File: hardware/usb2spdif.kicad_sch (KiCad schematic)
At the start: 18 parts, among them J1 USB_C_Receptacle_USB2.0_16P, U1 RP2040, U2 W25Q16JVSS, U3 AP130-33Y, Y1 12MHz

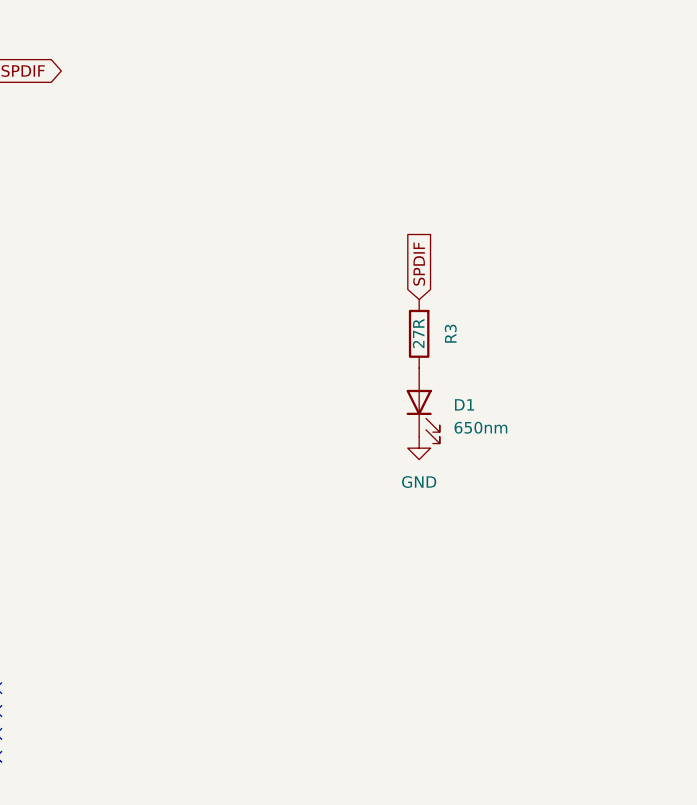
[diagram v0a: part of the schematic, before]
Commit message: [PCB] add real toslink TX and S/PDIF coax to schematic
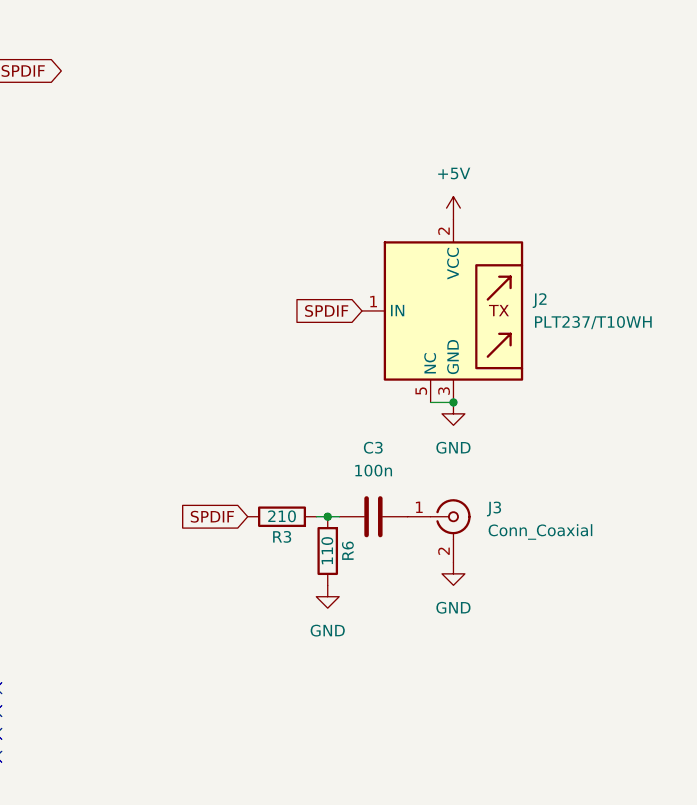
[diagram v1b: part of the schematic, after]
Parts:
- removed D1: 650nm, LED_THT:LED_D3.0mm_Horizontal_O1.27mm_Z2.0mm_Clear, symbol Device:LED
- added C3: 100n, symbol Device:C
- added J2: PLT237/T10WH, symbol spdif_tx:EVERLIGHT PLT237/T10WH
- added J3: Conn_Coaxial, symbol Connector:Conn_Coaxial
- added R6: 110, Resistor_SMD:R_0603_1608Metric, symbol Device:R
- R3: value 27R -> 210
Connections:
- net +5V: now also J2.2 (VCC)
- net GND: now also J2.3 (GND), J2.4 (NC), J2.5 (NC), J3.2 (Ext), R6.1
- net SPDIF: now also R3.1, J2.1 (IN); no longer R3.2
- new net: C3.1, R3.2, R6.2
- new net: C3.2, J3.1 (In)

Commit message: [PCB] forgot to commit that
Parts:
- added SW1: TS-1088-xR025, Button_Switch_SMD:SW_SPST_TS-1088-xR025, symbol Switch:SW_Push
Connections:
- net FLASH_CS: now also SW1.2
- net GND: now also SW1.1
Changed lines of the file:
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@@
+	(wire
+		(pts
+			(xy 58.42 185.42) (xy 49.53 185.42)
+		)
+		(stroke
+			(width 0)
+			(type default)
+		)
+	)
 	(wire
 		(pts
@@
 		)
 	)
+	(label "FLASH_CS"
+		(at 58.42 185.42 180)
+		(effects
+			(font
+				(size 1.27 1.27)
+			)
+			(justify right bottom)
+		)
+	)
 	(label "FLASH_CK"
 		(at 66.04 100.33 180)
@@
 	)
 	(symbol
+		(lib_id "power:GND")
+		(at 39.37 185.42 270)
+		(unit 1)
+		(exclude_from_sim no)
+		(in_bom yes)
+		(on_board yes)
+		(dnp no)
+		(fields_autoplaced yes)
+		(property "Reference" "#PWR018"
+			(at 33.02 185.42 0)
+			(effects
+				(font
+					(size 1.27 1.27)
+				)
+				(hide yes)
+			)
+		)
+		(property "Value" "GND"
+			(at 35.56 185.4199 90)
+			(effects
+				(font
+					(size 1.27 1.27)
+				)
+				(justify right)
+			)
+		)
+		(property "Footprint" ""
+			(at 39.37 185.42 0)
+			(effects
+				(font
+					(size 1.27 1.27)
+				)
+				(hide yes)
+			)
+		)
+		(property "Datasheet" ""
+			(at 39.37 185.42 0)
+			(effects
+				(font
+					(size 1.27 1.27)
+				)
+				(hide yes)
+			)
+		)
+		(property "Description" "Power symbol creates a global label with name \"GND\" , ground"
+			(at 39.37 185.42 0)
+			(effects
+				(font
+					(size 1.27 1.27)
+				)
+				(hide yes)
+			)
+		)
+		(pin "1"
+		)
+		(instances
+			(project "usb2spdif"
+				(path "/b44cd5a2-fc79-4a91-bdf7-b405b0b9808b"
+					(reference "#PWR018")
+					(unit 1)
+				)
+			)
+		)
+	)
+	(symbol
 		(lib_id "Device:C")
 		(at 50.8 158.75 0)
@@
 					(unit 1)
 				)
+			)
+		)
+	)
+	(symbol
+		(lib_id "Switch:SW_Push")
+		(at 44.45 185.42 0)
+		(unit 1)
+		(exclude_from_sim no)
+		(in_bom yes)
+		(on_board yes)
+		(dnp no)
+		(fields_autoplaced yes)
+		(property "Reference" "SW1"
+			(at 44.45 177.8 0)
+			(effects
+				(font
+					(size 1.27 1.27)
+				)
+			)
+		)
+		(property "Value" "TS-1088-xR025"
+			(at 44.45 180.34 0)
+			(effects
+				(font
+					(size 1.27 1.27)
+				)
+			)
+		)
+		(property "Footprint" "Button_Switch_SMD:SW_SPST_TS-1088-xR025"
+			(at 44.45 180.34 0)
+			(effects
+				(font
+					(size 1.27 1.27)
+				)
+				(hide yes)
+			)
+		)
+		(property "Datasheet" "~"
+			(at 44.45 180.34 0)
+			(effects
+				(font
+					(size 1.27 1.27)
+				)
+				(hide yes)
+			)
+		)
+		(property "Description" "Push button switch, generic, two pins"
+			(at 44.45 185.42 0)
+			(effects
+				(font
+					(size 1.27 1.27)
+				)
+				(hide yes)
+			)
+		)
+		(pin "2"
+		)
+		(pin "1"
+		)
+		(instances
+			(project ""
+				(path "/b44cd5a2-fc79-4a91-bdf7-b405b0b9808b"
+					(reference "SW1")
+					(unit 1)
+				)
